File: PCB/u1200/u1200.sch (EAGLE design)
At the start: 119 parts, among them IC1 74LS74D, J1 ATX24RH, P1 CBM_A1200_EDGE_CONNECTOR, U16 DRAM_256KX16, U17 DRAM_256KX16, U18 DRAM_256KX16, U19 DRAM_256KX16, U2 CBM_8374, U20 CBM_391425, U4 CBM_4203, U6A AM29F400S, U6B AM29F400S

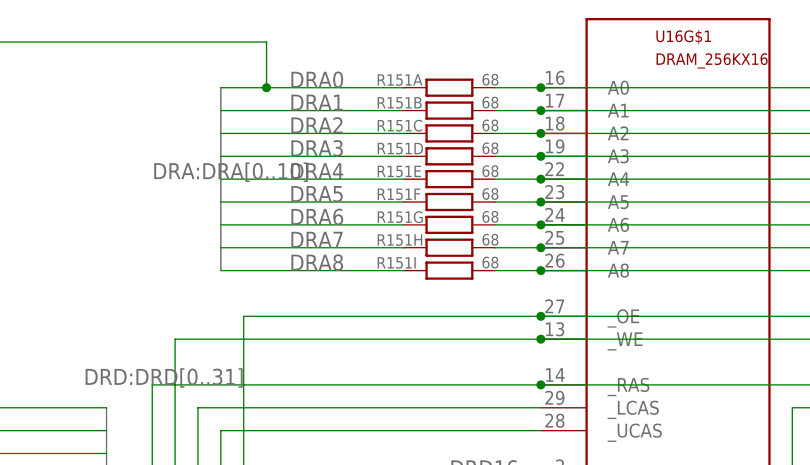
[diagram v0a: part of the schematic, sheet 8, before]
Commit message: A and DRA bus manual routing
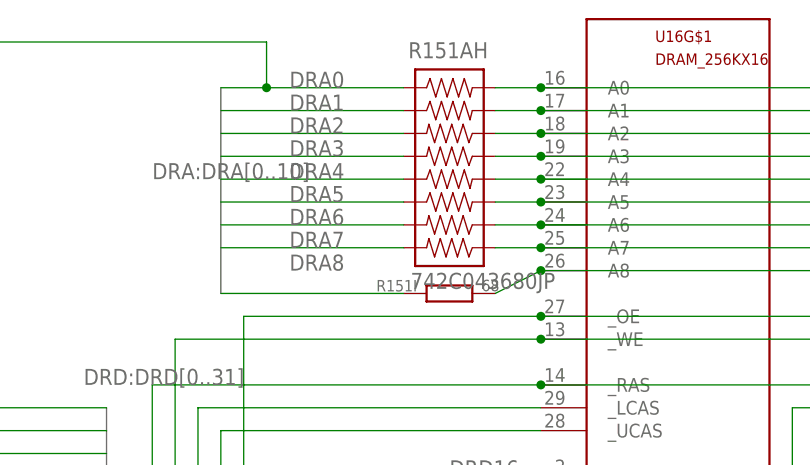
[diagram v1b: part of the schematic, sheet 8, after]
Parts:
- removed R151A, R151B, R151C, R151D, R151E, R151F, R151G, R151H: 68, rcl:R-EU_R0805
- added R151AH: 742C043680JP, Resistor Array:742C163220JP
- R151I: device rcl:R-EU_R0805 -> rcl:R-EU_R0603
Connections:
- net A17: now also U6AG$1.A17; no longer U6AG$1.A16
- net A18: now also U6AG$1.A16
- net A19: no longer U6AG$1.A17
- net BDRA0: now also R151AH.16; no longer R151A.2
- net BDRA1: now also R151AH.15; no longer R151B.2
- net BDRA2: now also R151AH.14; no longer R151C.2
- net BDRA3: now also R151AH.13; no longer R151D.2
- net BDRA4: now also R151AH.12; no longer R151E.2
- net BDRA5: now also R151AH.11; no longer R151F.2
- net BDRA6: now also R151AH.10; no longer R151G.2
- net BDRA7: now also R151AH.9; no longer R151H.2
- net DRA0: now also R151AH.1; no longer R151A.1
- net DRA1: now also R151AH.2; no longer R151B.1
- net DRA2: now also R151AH.3; no longer R151C.1
- net DRA3: now also R151AH.4; no longer R151D.1
- net DRA4: now also R151AH.5; no longer R151E.1
- net DRA5: now also R151AH.6; no longer R151F.1
- net DRA6: now also R151AH.7; no longer R151G.1
- net DRA7: now also R151AH.8; no longer R151H.1
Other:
- moved on the sheet: R151I

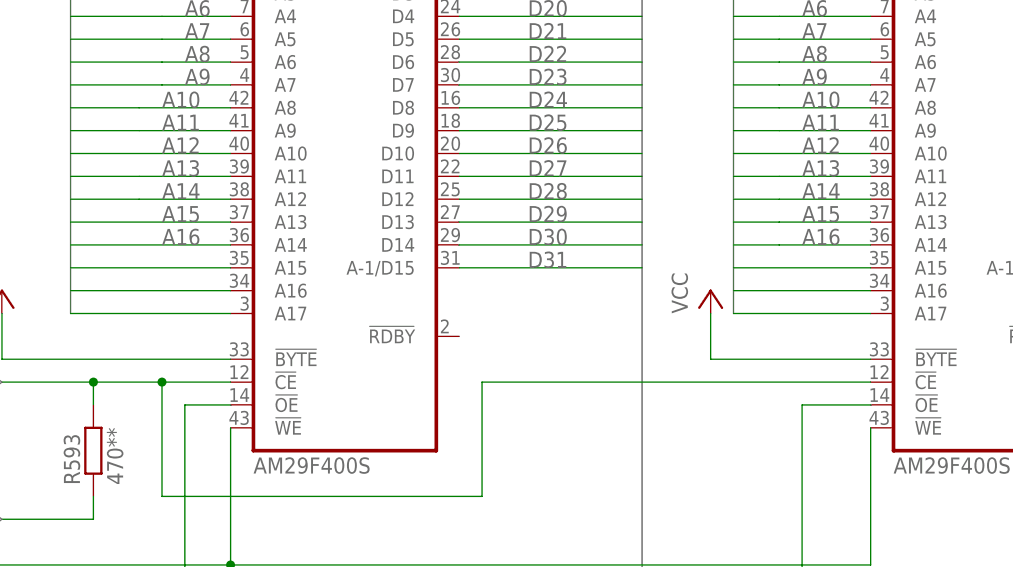
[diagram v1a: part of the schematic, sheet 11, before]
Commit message: a0-a20 bus from edge connector to chip ram
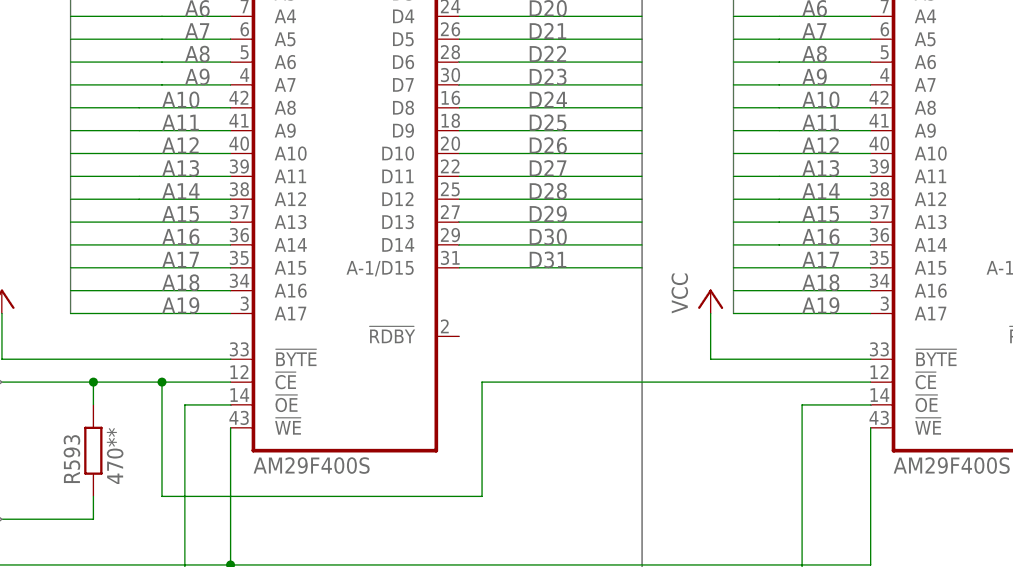
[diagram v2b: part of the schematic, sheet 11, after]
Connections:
- net A17: no longer U6AG$1.A17
- net A19: now also U6AG$1.A17
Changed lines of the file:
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@@
 <pinref part="U6A" gate="G$1" pin="A15"/>
 <wire x1="170.18" y1="96.52" x2="187.96" y2="96.52" width="0.1524" layer="91"/>
-</segment>
-<segment>
-<pinref part="U6A" gate="G$1" pin="A17"/>
-<wire x1="170.18" y1="91.44" x2="187.96" y2="91.44" width="0.1524" layer="91"/>
+<label x="180.34" y="96.52" size="1.778" layer="95"/>
 </segment>
 <segment>
 <pinref part="U6B" gate="G$1" pin="A15"/>
 <wire x1="243.84" y1="96.52" x2="259.08" y2="96.52" width="0.1524" layer="91"/>
+<label x="251.46" y="96.52" size="1.778" layer="95"/>
 </segment>
 </net>
@@
 <pinref part="U6A" gate="G$1" pin="A16"/>
 <wire x1="170.18" y1="93.98" x2="187.96" y2="93.98" width="0.1524" layer="91"/>
+<label x="180.34" y="93.98" size="1.778" layer="95"/>
 </segment>
 <segment>
 <pinref part="U6B" gate="G$1" pin="A16"/>
 <wire x1="243.84" y1="93.98" x2="259.08" y2="93.98" width="0.1524" layer="91"/>
+<label x="251.46" y="93.98" size="1.778" layer="95"/>
 </segment>
 </net>
@@
 <pinref part="U6B" gate="G$1" pin="A17"/>
 <wire x1="243.84" y1="91.44" x2="259.08" y2="91.44" width="0.1524" layer="91"/>
+<label x="251.46" y="91.44" size="1.778" layer="95"/>
+</segment>
+<segment>
+<pinref part="U6A" gate="G$1" pin="A17"/>
+<wire x1="170.18" y1="91.44" x2="187.96" y2="91.44" width="0.1524" layer="91"/>
+<label x="180.34" y="91.44" size="1.778" layer="95"/>
 </segment>
 </net>

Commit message: Added License
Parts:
- removed R951A, R951B, R951C, R951D, R951E, R951F, R951G: 4.7K, rcl:R-EU_R0805
- added R951AG: 741X163220JP, Resistor Array:741X163220JP
- R593: device rcl:R-EU_R0805 -> rcl:R-EU_R0603
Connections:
- net GND: no longer P1.SYSTEM_0, P1.SYSTEM_1, P1._CONFIG_OUT
- net R_W: now also R951AG.5; no longer R951E.1
- net SIZE_0: now also R951AG.3; no longer R951C.1
- net SIZE_1: now also R951AG.4; no longer R951D.1
- net VCC: now also R951AG.10, R951AG.11, R951AG.12, R951AG.13, R951AG.14, R951AG.15, R951AG.16; no longer R951A.2, R951B.2, R951C.2, R951D.2, R951E.2, R951F.2, R951G.2
- net _AS: now also R951AG.6; no longer R951F.1
- net _DS: now also R951AG.7; no longer R951G.1
- net _HLT: now also R951AG.1; no longer R951A.1
- net _RST: now also R951AG.2; no longer R951B.1
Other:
- note added: "4.7k"
- note added: "This work is licensed under the Creative Commons Attribution-ShareAlike 4.0 International License. To view a copy of this license, visit http://creativecommons.org/licenses/by-sa/4.0/ or send a letter to Creative Commons, PO Box 1866, Mountain View, CA 94042, USA."

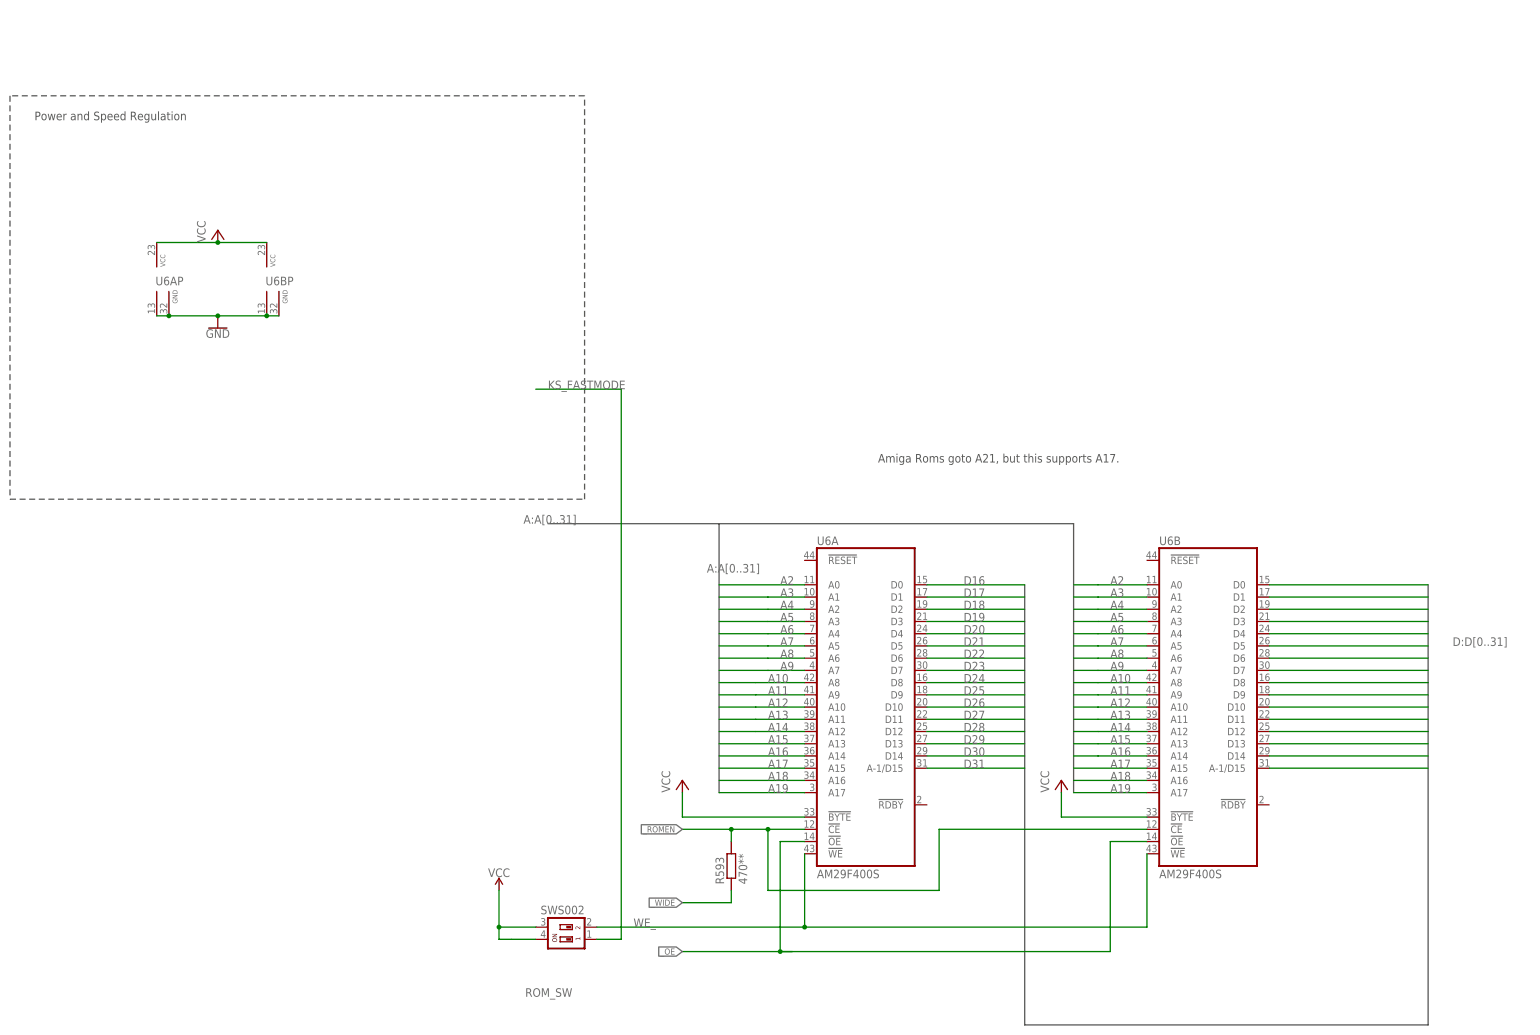
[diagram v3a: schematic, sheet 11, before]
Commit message: Changed ROMs more traditional format. Re-routed A bus
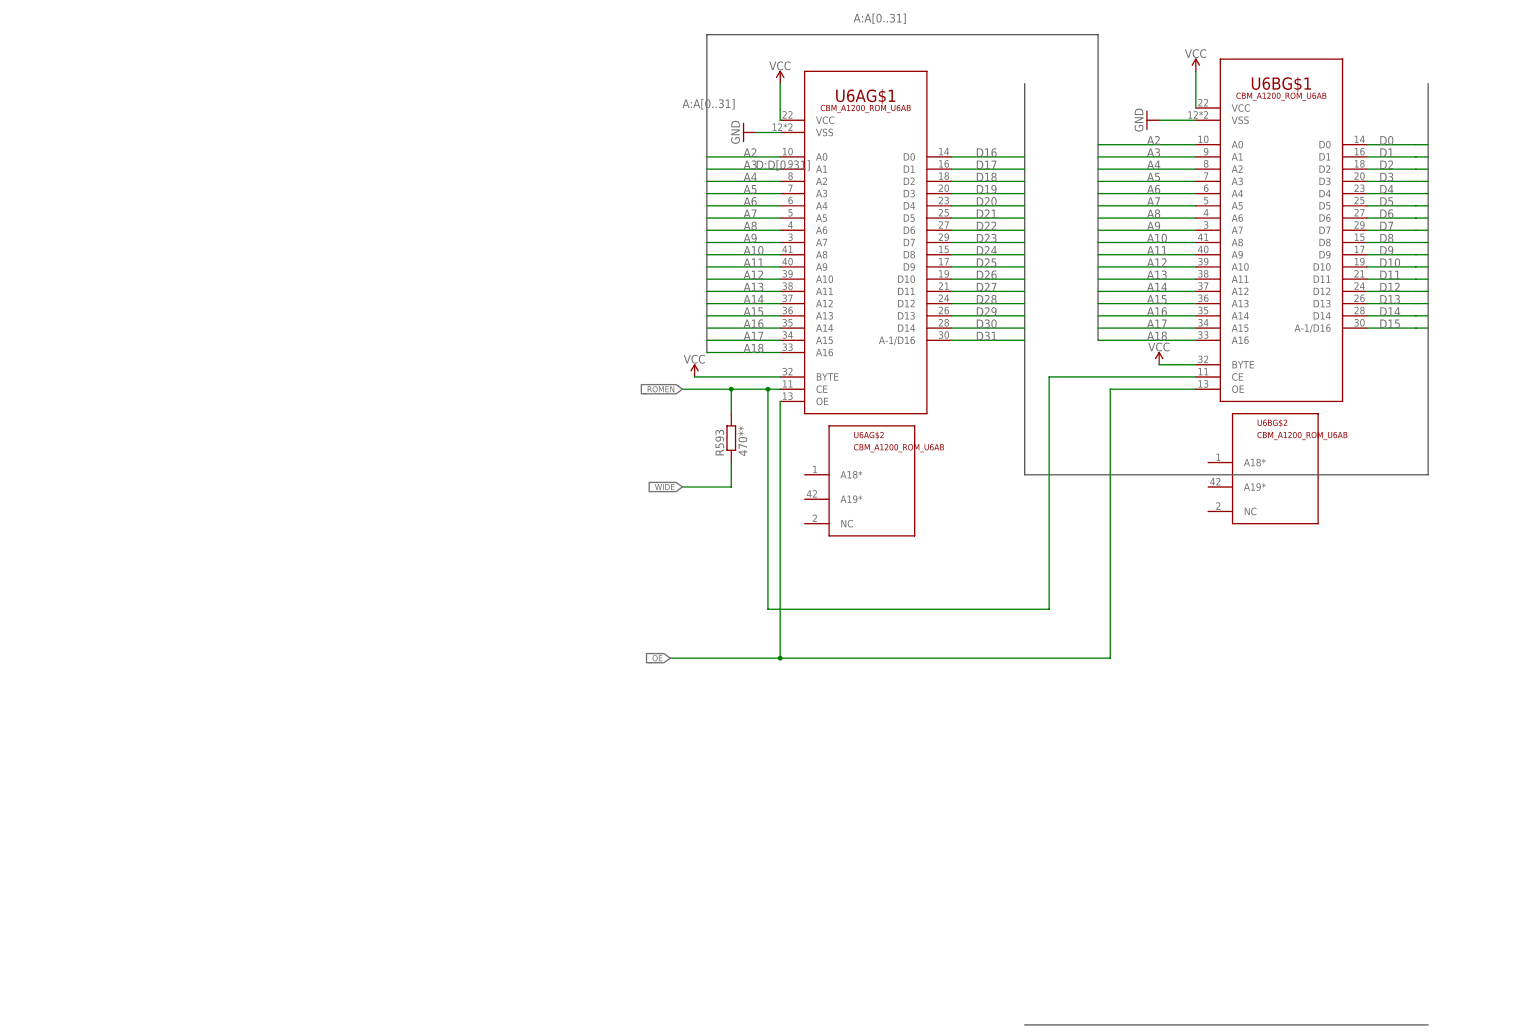
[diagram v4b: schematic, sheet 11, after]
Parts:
- removed R101, R103, R952A, R952B, R953A, R953B, R953C: 470, rcl:R-EU_R0805
- removed ROM_SW: SWS002, smd-special:SWS002
- added R101_104_952AB: 741X163220JP, Resistor Array:741X163220JP
- U6A, U6B: value AM29F400S -> CBM_A1200_ROM_U6AB; device am29-memory:AM29F400S -> u1200:CBM_A1200_ROM_U6AB
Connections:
- removed net KS_FASTMODE: ROM_SW.1
- removed net WE_: ROM_SW.2, U6AG$1.!WE, U6BG$1.!WE
- net A19: no longer U6AG$1.A17, U6BG$1.A17
- net D15: now also U6BG$1.A-1/D16; no longer U6BG$1.A-1/D15
- net D31: now also U6AG$1.A-1/D16; no longer U6AG$1.A-1/D15
- net GND: now also U6AG$1.VSS, U6BG$1.VSS; no longer U6AP.GND@1, U6AP.GND@2, U6BP.GND@1, U6BP.GND@2
- net IPL0: now also R101_104_952AB.1; no longer R953A.1
- net IPL1: now also R101_104_952AB.2; no longer R953B.1
- net IPL2: now also R101_104_952AB.3; no longer R953C.1
- net R_W: now also R951AG.8; no longer R951AG.5
- net SIZE_0: now also R951AG.5; no longer R951AG.3
- net VCC: now also R101_104_952AB.10, R101_104_952AB.11, R101_104_952AB.12, R101_104_952AB.13, R101_104_952AB.14, R101_104_952AB.15, R101_104_952AB.16, R951AG.9, U6AG$1.BYTE, U6AG$1.VCC, U6BG$1.BYTE, U6BG$1.VCC; no longer R101.2, R103.2, R952A.2, R952B.2, R953A.2, R953B.2, R953C.2, ROM_SW.3, ROM_SW.4, U6AG$1.!BYTE, U6AP.VCC, U6BG$1.!BYTE, U6BP.VCC
- net _AVEC: now also R101_104_952AB.5; no longer R103.1
- net _BEER: now also R101_104_952AB.4; no longer R101.1
- net _DSACK_0: now also R101_104_952AB.6; no longer R952A.1
- net _DSACK_1: now also R101_104_952AB.7; no longer R952B.1
- net _HLT: now also R951AG.2; no longer R951AG.1
- net _OE: now also U6AG$1.OE, U6BG$1.OE; no longer U6AG$1.!OE, U6BG$1.!OE
- net _ROMEN: now also U6AG$1.CE, U6BG$1.CE; no longer U6AG$1.!CE, U6BG$1.!CE
- net _RST: now also R951AG.3; no longer R951AG.2
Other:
- note added: "470"
- note removed: "Amiga Roms goto A21, but this supports A17."
- note removed: "Power and Speed Regulation"
- moved on the sheet: R593
